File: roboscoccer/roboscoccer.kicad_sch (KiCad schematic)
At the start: 17 parts, among them J1 HC-05, J2 motordriver 1 2, J3 solar conn, J6 motordriver 3 4, U1 Buck

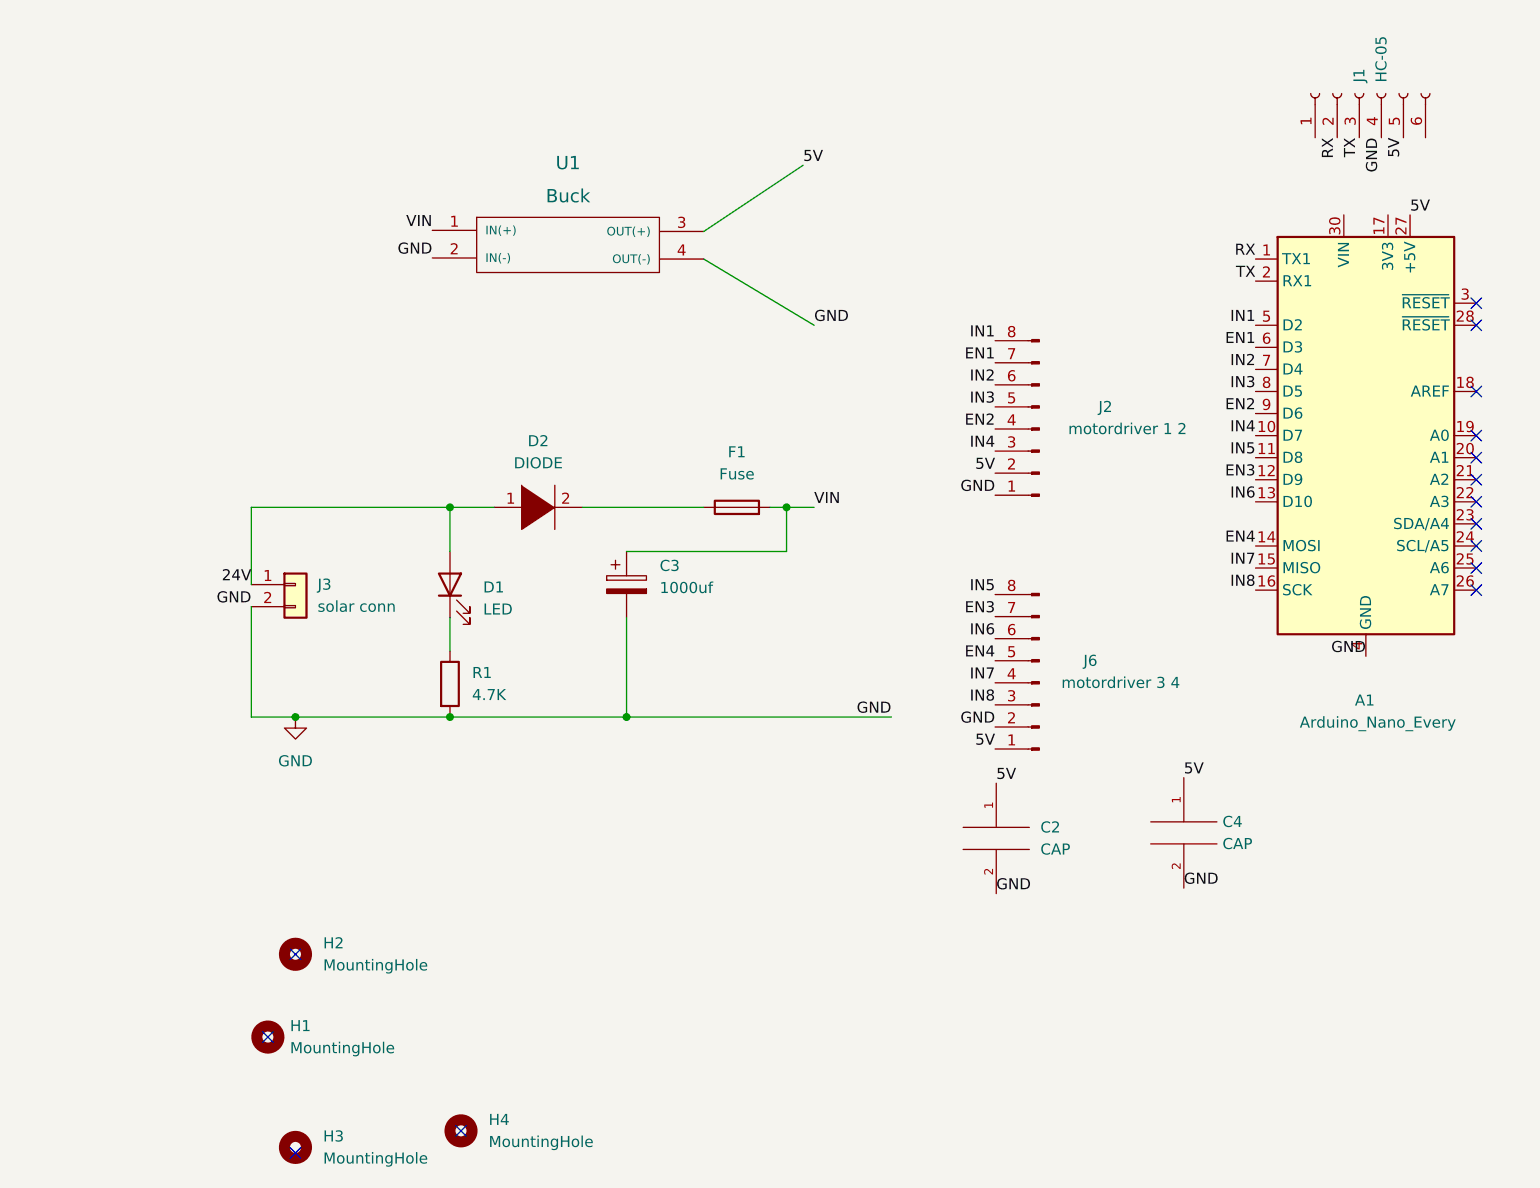
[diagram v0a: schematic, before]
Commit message: Position of power supply components changed
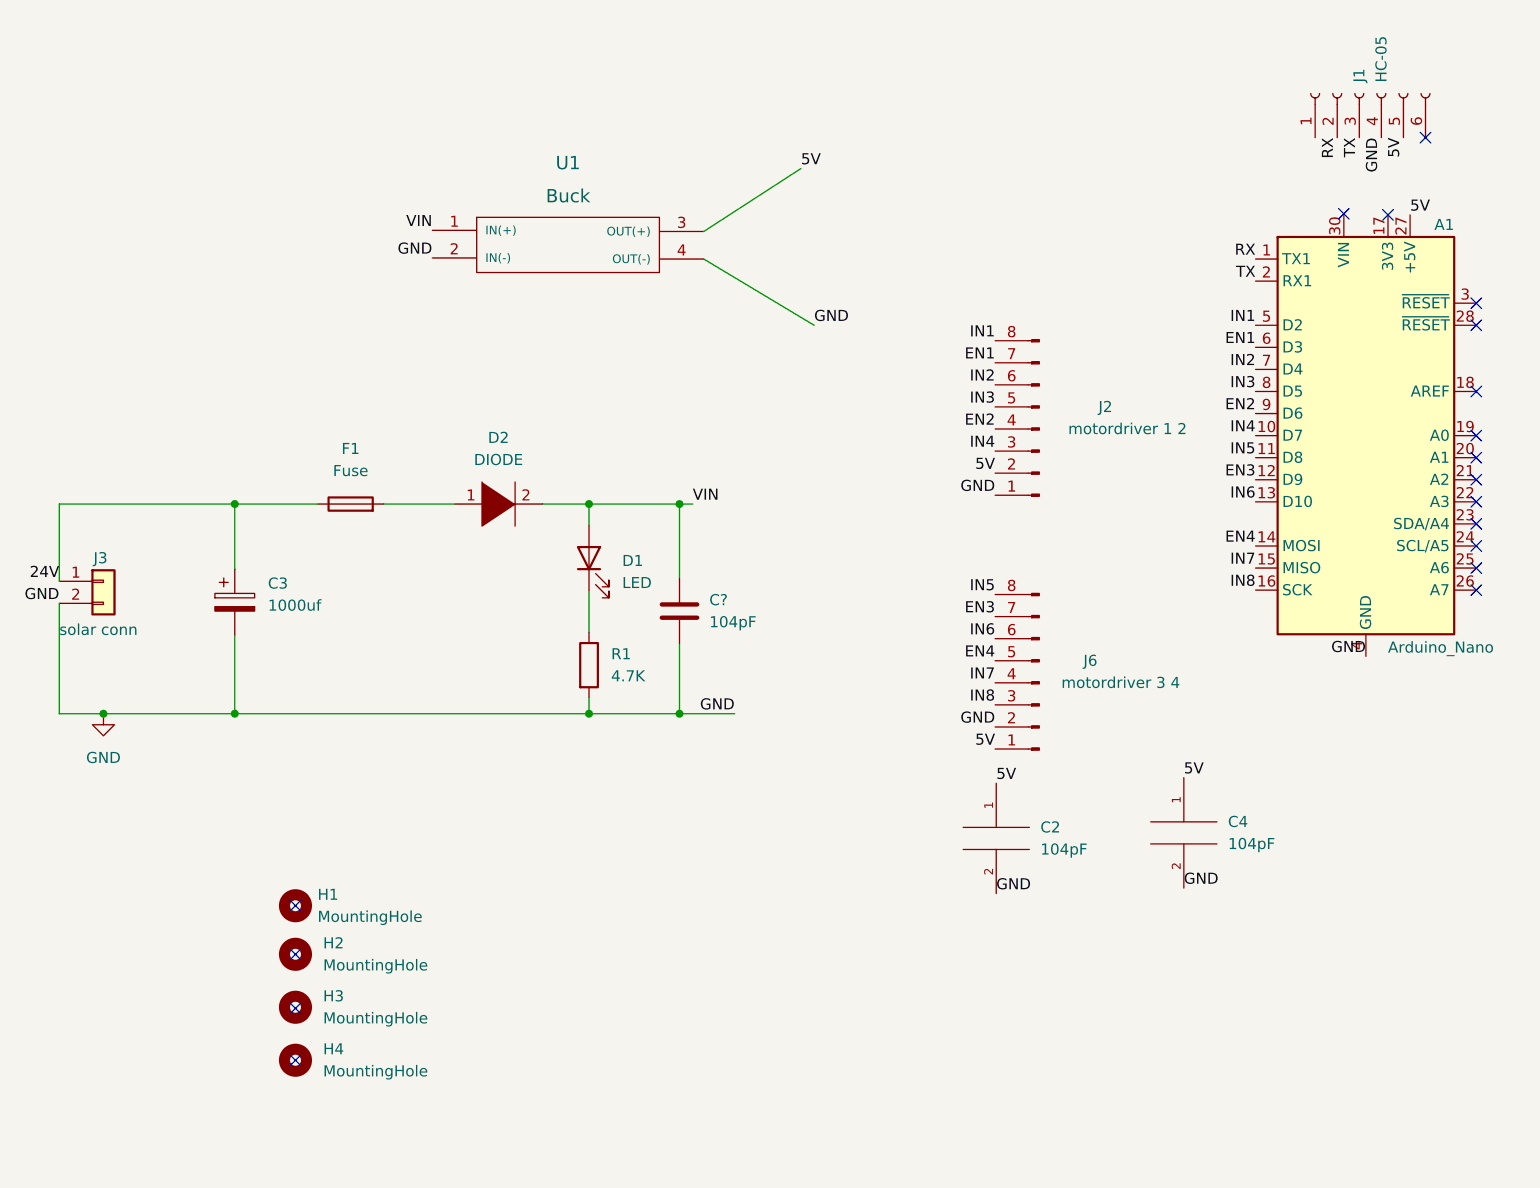
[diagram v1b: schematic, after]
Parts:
- added C?: 104pF, symbol Device:C
- A1: value Arduino_Nano_Every -> Arduino_Nano
- C2, C4: value CAP -> 104pF
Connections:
- net 24V: now also C3.1, F1.1; no longer D1.2 (A), D2.1 (K)
- net GND: now also C?.2
- net VIN: now also D1.2 (A), D2.2 (A), C?.1; no longer C3.1, F1.2
- new net: D2.1 (K), F1.2
- no-connect marks 15 -> 18
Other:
- moved on the sheet: C3, D1, D2, F1, H1, H3, H4, J3, R1

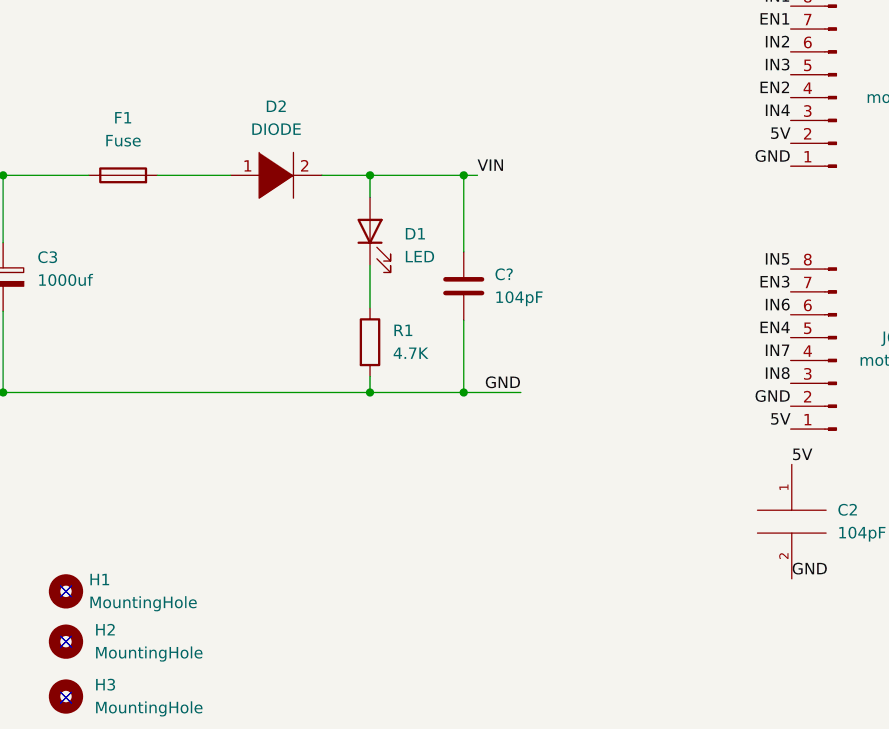
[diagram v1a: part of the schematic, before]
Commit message: Decoupling capacitors placement near 5V power output
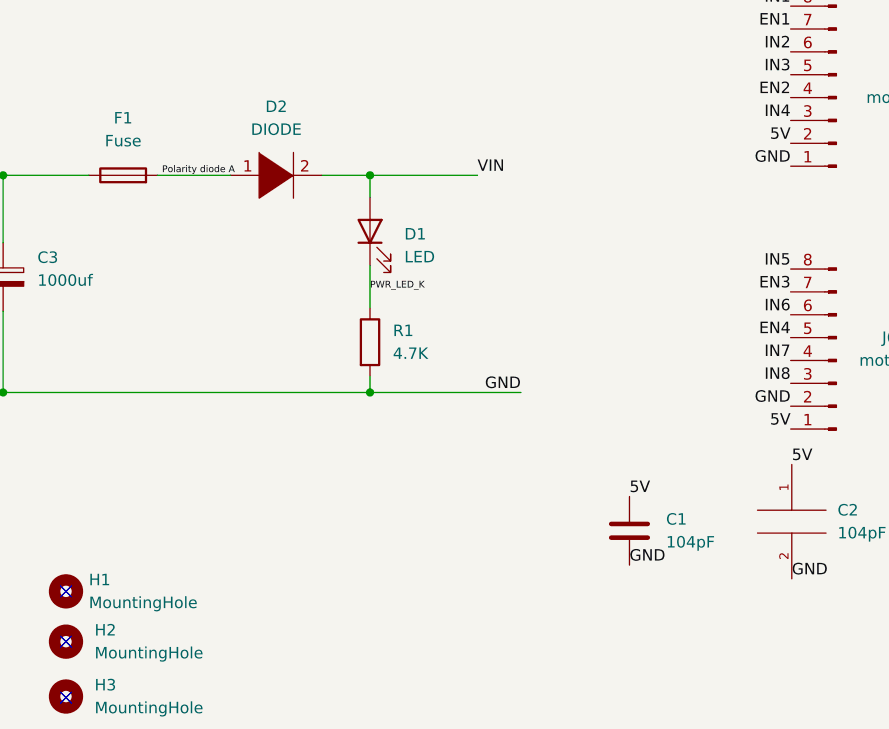
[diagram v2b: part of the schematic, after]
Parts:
- C1: renamed from C?; footprint (none) -> MY_LIB:Capacitor_Disc_Small
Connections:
- net 5V: now also C1.1
- net VIN: no longer C1.1
- net Polarity diode A: now reaches D2.1 (K), F1.2
- net PWR_LED_K: now reaches D1.1 (K), R1.1
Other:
- moved on the sheet: C1
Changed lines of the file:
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@@
   (junction (at 105.537 110.744) (diameter 0) (color 0 0 0 0)
   )
-  (junction (at 115.951 110.744) (diameter 0) (color 0 0 0 0)
-  )
   (junction (at 64.77 110.744) (diameter 0) (color 0 0 0 0)
-  )
-  (junction (at 115.951 134.874) (diameter 0) (color 0 0 0 0)
   )
   (junction (at 49.657 134.874) (diameter 0) (color 0 0 0 0)
@@
     (stroke (width 0) (type default) (color 0 0 0 0))
   )
-  (wire (pts (xy 115.951 126.873) (xy 115.951 134.874))
-    (stroke (width 0) (type default) (color 0 0 0 0))
-  )
-  (wire (pts (xy 105.537 110.744) (xy 115.951 110.744))
-    (stroke (width 0) (type default) (color 0 0 0 0))
-  )
   (wire (pts (xy 44.577 119.634) (xy 44.577 110.744))
     (stroke (width 0) (type default) (color 0 0 0 0))
@@
     (stroke (width 0) (type default) (color 0 0 0 0))
   )
-  (wire (pts (xy 105.537 134.874) (xy 115.951 134.874))
-    (stroke (width 0) (type default) (color 0 0 0 0))
-  )
-  (wire (pts (xy 115.951 134.874) (xy 122.301 134.874))
+  (wire (pts (xy 105.537 134.874) (xy 122.301 134.874))
     (stroke (width 0) (type default) (color 0 0 0 0))
   )
@@
     (stroke (width 0) (type default) (color 0 0 0 0))
   )
-  (wire (pts (xy 115.951 110.744) (xy 117.475 110.744))
+  (wire (pts (xy 105.537 110.744) (xy 117.475 110.744))
     (stroke (width 0) (type default) (color 0 0 0 0))
   )
@@
     (stroke (width 0) (type default) (color 0 0 0 0))
   )
-  (wire (pts (xy 115.951 110.744) (xy 115.951 119.253))
-    (stroke (width 0) (type default) (color 0 0 0 0))
-  )
   (label "5V" (at 152.4 142.875 0)
     (effects (font (size 1.27 1.27)) (justify left bottom))
@@
     (effects (font (size 1.27 1.27)) (justify right bottom))
   )
+  (label "PWR_LED_K" (at 105.537 123.571 0)
+    (effects (font (size 0.75 0.75)) (justify left bottom))
+  )
   (label "5V" (at 173.99 142.24 0)
     (effects (font (size 1.27 1.27)) (justify left bottom))
@@
     (effects (font (size 1.27 1.27)) (justify right bottom))
   )
+  (label "GND" (at 134.366 154.051 0)
+    (effects (font (size 1.27 1.27)) (justify left bottom))
+  )
   (label "IN6" (at 152.273 126.238 180)
     (effects (font (size 1.27 1.27)) (justify right bottom))
@@
     (effects (font (size 1.27 1.27)) (justify right bottom))
   )
+  (label "Polarity diode A" (at 82.423 110.744 0)
+    (effects (font (size 0.75 0.75)) (justify left bottom))
+  )
   (label "GND" (at 194.945 128.27 180)
     (effects (font (size 1.27 1.27)) (justify right bottom))
+  )
+  (label "5V" (at 134.366 146.431 0)
+    (effects (font (size 1.27 1.27)) (justify left bottom))
   )
   (label "EN4" (at 182.245 115.57 180)
@@
     )
   )
-  (symbol (lib_id "Device:C") (at 115.951 123.063 0) (unit 1)
-    (in_bom yes) (on_board yes) (fields_autoplaced)
-    (property "Reference" "C?" (id 0) (at 119.38 121.7929 0)
-      (effects (font (size 1.27 1.27)) (justify left))
-    )
-    (property "Value" "104pF" (id 1) (at 119.38 124.3329 0)
-      (effects (font (size 1.27 1.27)) (justify left))
-    )
-    (property "Footprint" "" (id 2) (at 116.9162 126.873 0)
-      (effects (font (size 1.27 1.27)) hide)
-    )
-    (property "Datasheet" "~" (id 3) (at 115.951 123.063 0)
+  (symbol (lib_id "Device:C") (at 134.366 150.241 0) (unit 1)
+    (in_bom yes) (on_board yes) (fields_autoplaced)
+    (property "Reference" "C1" (id 0) (at 138.43 148.9709 0)
+      (effects (font (size 1.27 1.27)) (justify left))
+    )
+    (property "Value" "104pF" (id 1) (at 138.43 151.5109 0)
+      (effects (font (size 1.27 1.27)) (justify left))
+    )
+    (property "Footprint" "MY_LIB:Capacitor_Disc_Small" (id 2) (at 135.3312 154.051 0)
+      (effects (font (size 1.27 1.27)) hide)
+    )
+    (property "Datasheet" "~" (id 3) (at 134.366 150.241 0)
       (effects (font (size 1.27 1.27)) hide)
     )
@@
       (reference "A1") (unit 1) (value "Arduino_Nano") (footprint "MY_LIB:Arduino_Nano")
     )
+    (path "/bea64ee0-ff3b-4d5d-b254-4aa9253637eb"
+      (reference "C1") (unit 1) (value "104pF") (footprint "MY_LIB:Capacitor_Disc_Small")
+    )
     (path "/a79c0254-86d5-46ff-9add-51da4d3aa6f6"
       (reference "C2") (unit 1) (value "104pF") (footprint "MY_LIB:Capacitor_Disc_Small")
@@
       (reference "C4") (unit 1) (value "104pF") (footprint "MY_LIB:Capacitor_Disc_Small")
     )
-    (path "/bea64ee0-ff3b-4d5d-b254-4aa9253637eb"
-      (reference "C?") (unit 1) (value "104pF") (footprint "")
-    )
     (path "/78e43c23-87ae-4a80-a6a7-432e138b6912"
